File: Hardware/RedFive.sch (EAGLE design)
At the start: 95 parts, among them IC3 LM1117, J1 AVR_SPI_PROG_3X2PTH, J2 USB Female Type C Connector, J3 POWER_JACKSUPER_BOMB_DIGITY, J5 JTAG, Q1 1.1A/60V/600mΩ, U2 1.8V, U3 AP2112-3.3V, U4 FE310, U5 32MB, Y1 32.768KHZ, Y2 16MHz

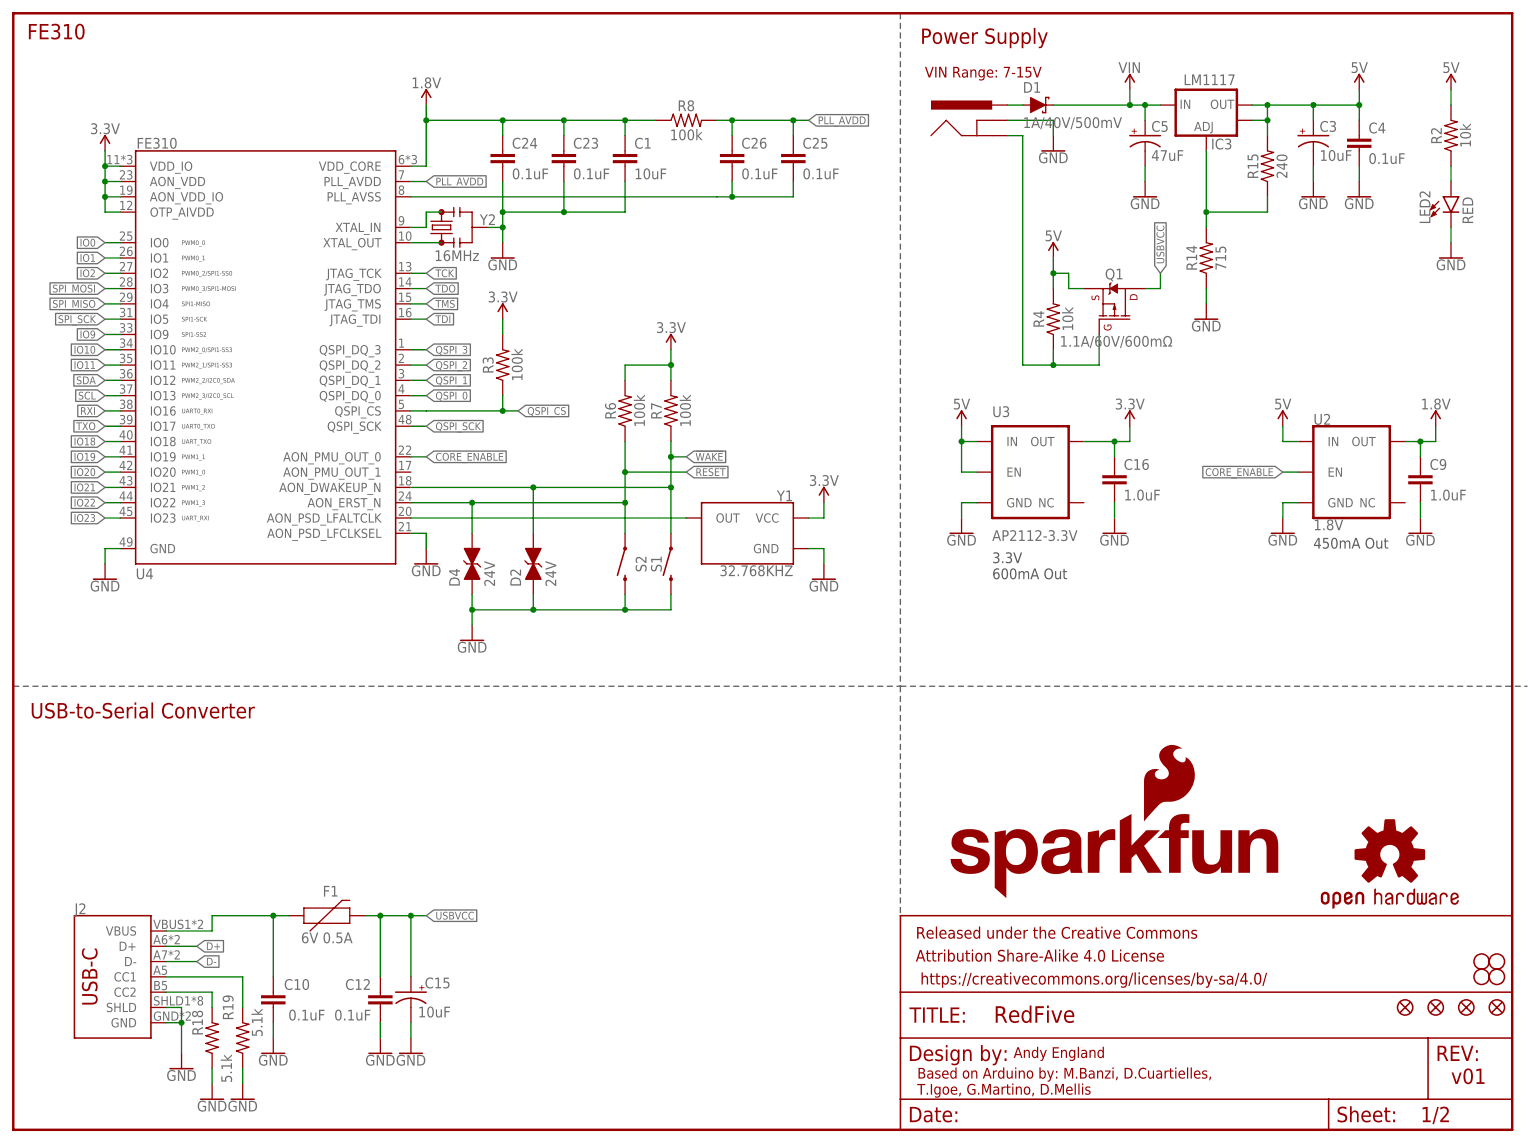
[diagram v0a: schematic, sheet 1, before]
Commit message: small schematic tweaks, thanks pete for notes
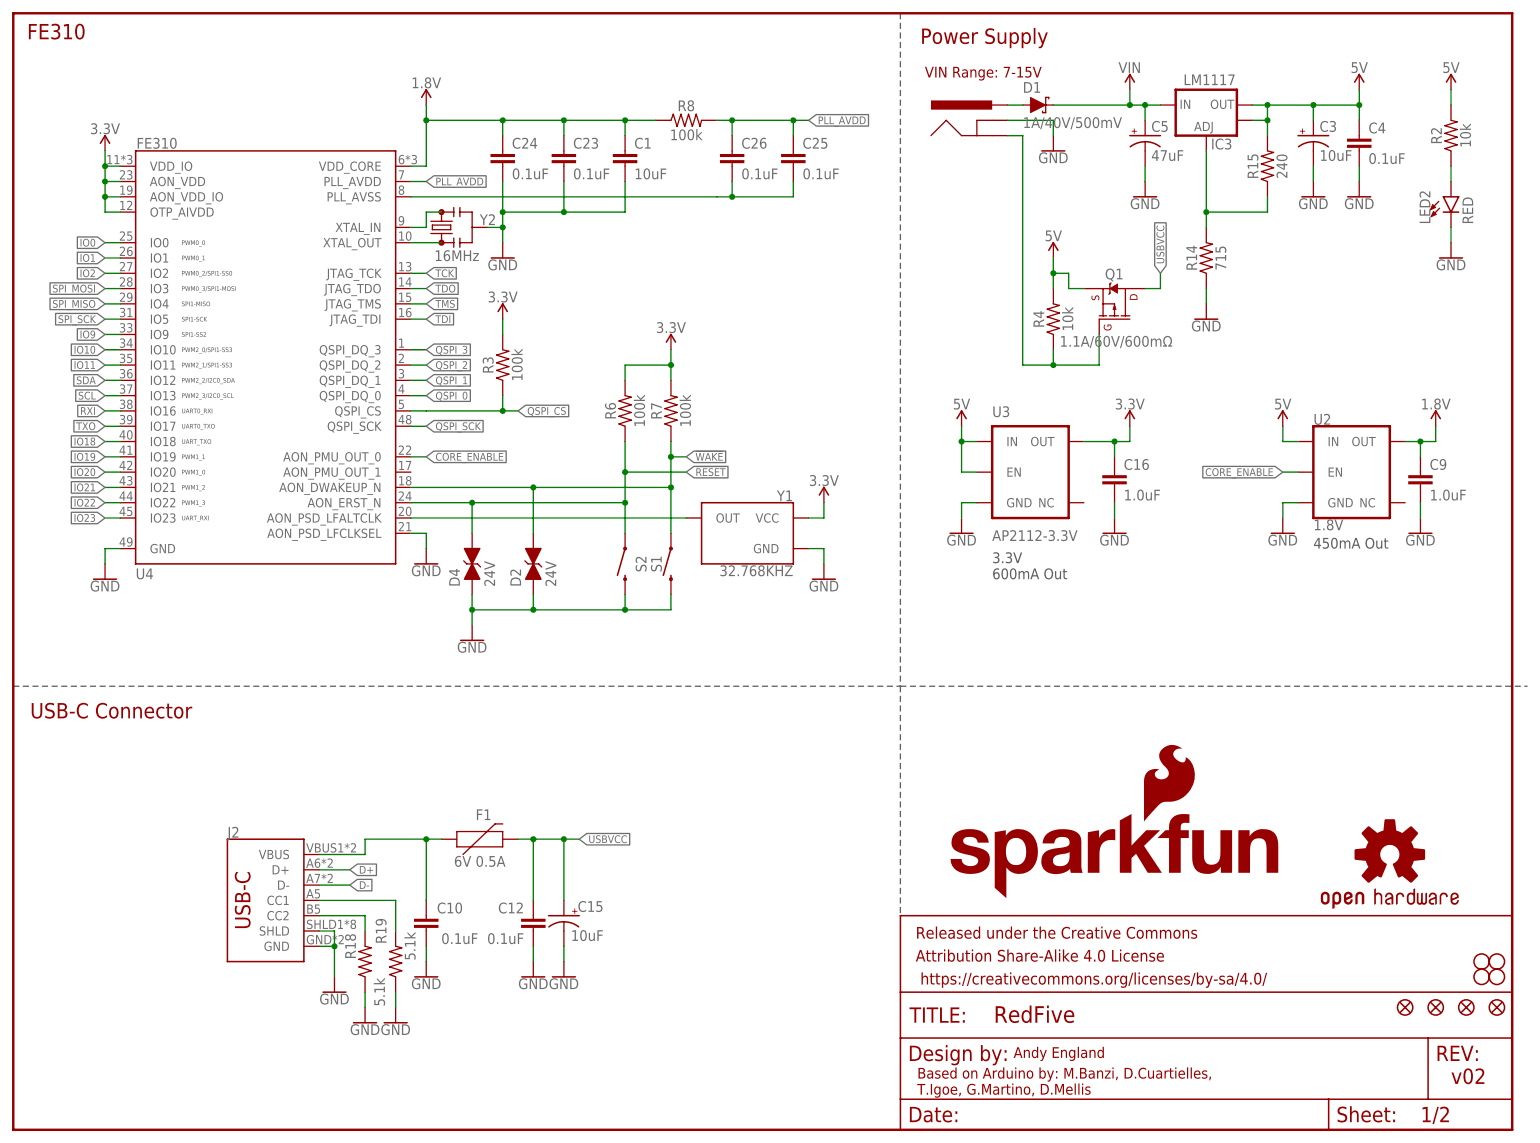
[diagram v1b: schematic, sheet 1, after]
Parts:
- J1: value AVR_SPI_PROG_3X2PTH -> FEMALE 2x3; device SparkFun-Connectors:AVR_SPI_PROG_3X2PTH -> SparkFun-Connectors:CONN_03X2FEMALE
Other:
- note added: "USB-C Connector"
- note removed: "USB-to-Serial Converter"
- note removed: "v01"
- moved on the sheet: C10, C12, C15, F1, J2, R18, R19

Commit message: post design review changes
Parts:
- added JP1: JUMPER-SMT_2_NO_NO-SILK, SparkFun-Jumpers:JUMPER-SMT_2_NO_NO-SILK
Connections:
- net USBVCC: now also JP1.2
- net VUSB: now also JP1.1
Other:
- note added: "Closing this jumper bypasses the .5A fuse. Only close it if you need a lot of current."
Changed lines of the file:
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@@
 <part name="GND27" library="SparkFun-PowerSymbols" deviceset="GND" device=""/>
 <part name="SUPPLY23" library="SparkFun-PowerSymbols" deviceset="3.3V" device=""/>
+<part name="JP1" library="SparkFun-Jumpers" deviceset="JUMPER-SMT_2_NO" device="_NO-SILK"/>
 </parts>
 <sheets>
@@
 <wire x1="147.32" y1="185.42" x2="147.32" y2="73.66" width="0.2032" layer="97" style="longdash"/>
 <text x="215.9" y="96.52" size="1.778" layer="97" font="vector">450mA Out</text>
+<text x="15.24" y="60.96" size="1.778" layer="94" font="vector">Closing this jumper bypasses the .5A fuse. Only close it if you need a lot of current.</text>
 </plain>
 <instances>
@@
 <attribute name="VALUE" x="63.5" y="17.526" size="1.778" layer="96" align="top-center"/>
 </instance>
+<instance part="JP1" gate="G$1" x="76.2" y="55.88"/>
 </instances>
 <busses>
@@
 <pinref part="C15" gate="G$1" pin="+"/>
 <wire x1="83.82" y1="48.26" x2="86.36" y2="48.26" width="0.1524" layer="91"/>
-<wire x1="86.36" y1="48.26" x2="91.44" y2="48.26" width="0.1524" layer="91"/>
+<wire x1="86.36" y1="48.26" x2="88.9" y2="48.26" width="0.1524" layer="91"/>
+<wire x1="88.9" y1="48.26" x2="91.44" y2="48.26" width="0.1524" layer="91"/>
 <wire x1="91.44" y1="38.1" x2="91.44" y2="48.26" width="0.1524" layer="91"/>
 <pinref part="C12" gate="G$1" pin="1"/>
@@
 <wire x1="91.44" y1="48.26" x2="93.98" y2="48.26" width="0.1524" layer="91"/>
 <junction x="91.44" y="48.26"/>
+<pinref part="JP1" gate="G$1" pin="2"/>
+<wire x1="81.28" y1="55.88" x2="88.9" y2="55.88" width="0.1524" layer="91"/>
+<wire x1="88.9" y1="55.88" x2="88.9" y2="48.26" width="0.1524" layer="91"/>
+<junction x="88.9" y="48.26"/>
 </segment>
 </net>
@@
 <wire x1="50.8" y1="45.72" x2="58.42" y2="45.72" width="0.1524" layer="91"/>
 <wire x1="58.42" y1="45.72" x2="58.42" y2="48.26" width="0.1524" layer="91"/>
-<wire x1="58.42" y1="48.26" x2="68.58" y2="48.26" width="0.1524" layer="91"/>
+<wire x1="58.42" y1="48.26" x2="66.04" y2="48.26" width="0.1524" layer="91"/>
 <pinref part="C10" gate="G$1" pin="1"/>
+<wire x1="66.04" y1="48.26" x2="68.58" y2="48.26" width="0.1524" layer="91"/>
 <wire x1="68.58" y1="48.26" x2="71.12" y2="48.26" width="0.1524" layer="91"/>
 <wire x1="68.58" y1="38.1" x2="68.58" y2="48.26" width="0.1524" layer="91"/>
 <junction x="68.58" y="48.26"/>
 <pinref part="J2" gate="J1" pin="VBUS"/>
-</segment>
-</net>
+<wire x1="66.04" y1="48.26" x2="66.04" y2="55.88" width="0.1524" layer="91"/>
+<junction x="66.04" y="48.26"/>
+<pinref part="JP1" gate="G$1" pin="1"/>
+<wire x1="66.04" y1="55.88" x2="71.12" y2="55.88" width="0.1524" layer="91"/>
+</segment>
+</net>

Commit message: post checklist changes, protos ordered
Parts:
- removed TP8: TEST-POINT3, SparkFun-Connectors:TEST-POINT3
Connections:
- net DBG_RESET: no longer TP8.1
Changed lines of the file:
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@@
 <part name="SUPPLY18" library="SparkFun-PowerSymbols" deviceset="3.3V" device=""/>
 <part name="GND24" library="SparkFun-PowerSymbols" deviceset="GND" device=""/>
-<part name="TP8" library="SparkFun-Connectors" deviceset="TEST-POINT" device="3"/>
 <part name="R20" library="SparkFun-Resistors" deviceset="100KOHM" device="-0603-1/10W-1%" value="100k"/>
 <part name="SUPPLY19" library="SparkFun-PowerSymbols" deviceset="3.3V" device=""/>
@@
 <attribute name="VALUE" x="91.44" y="144.526" size="1.778" layer="96" align="top-center"/>
 </instance>
-<instance part="TP8" gate="G$1" x="157.48" y="40.64" smashed="yes" rot="R270">
-<attribute name="NAME" x="157.48" y="43.18" size="1.778" layer="95" font="vector" rot="R270"/>
-</instance>
 <instance part="R20" gate="G$1" x="160.02" y="53.34" smashed="yes" rot="R90">
 <attribute name="NAME" x="158.496" y="53.34" size="1.778" layer="95" font="vector" rot="R90" align="bottom-center"/>
@@
 <wire x1="160.02" y1="45.72" x2="157.48" y2="45.72" width="0.1524" layer="91"/>
 <junction x="160.02" y="45.72"/>
-<pinref part="TP8" gate="G$1" pin="1"/>
-<wire x1="157.48" y1="45.72" x2="157.48" y2="40.64" width="0.1524" layer="91"/>
 <wire x1="157.48" y1="45.72" x2="154.94" y2="45.72" width="0.1524" layer="91"/>
-<junction x="157.48" y="45.72"/>
 <label x="154.94" y="45.72" size="1.27" layer="95" font="vector" rot="R180" xref="yes"/>
 </segment>

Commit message: adding 5V test point
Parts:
- added TP8: TEST-POINT3, SparkFun-Connectors:TEST-POINT3
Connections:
- net 5V: now also TP8.1
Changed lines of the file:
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@@
 <part name="SUPPLY23" library="SparkFun-PowerSymbols" deviceset="3.3V" device=""/>
 <part name="JP1" library="SparkFun-Jumpers" deviceset="JUMPER-SMT_2_NO" device="_NO-SILK"/>
+<part name="TP8" library="SparkFun-Connectors" deviceset="TEST-POINT" device="3"/>
 </parts>
 <sheets>
@@
 <instance part="SUPPLY23" gate="G$1" x="20.32" y="81.28" smashed="yes">
 <attribute name="VALUE" x="20.32" y="84.074" size="1.778" layer="96" align="bottom-center"/>
+</instance>
+<instance part="TP8" gate="G$1" x="66.04" y="20.32" smashed="yes" rot="R180">
+<attribute name="NAME" x="68.58" y="20.32" size="1.778" layer="95" font="vector" rot="R180"/>
 </instance>
 </instances>
@@
 <segment>
 <pinref part="SUPPLY3" gate="G$1" pin="5V"/>
-<wire x1="73.66" y1="27.94" x2="73.66" y2="33.02" width="0.1524" layer="91"/>
 <pinref part="JP10" gate="G$1" pin="4"/>
 <wire x1="73.66" y1="20.32" x2="76.2" y2="20.32" width="0.1524" layer="91"/>
-<wire x1="73.66" y1="20.32" x2="73.66" y2="27.94" width="0.1524" layer="91"/>
-</segment>
-</net>
+<wire x1="73.66" y1="20.32" x2="73.66" y2="33.02" width="0.1524" layer="91"/>
+<pinref part="TP8" gate="G$1" pin="1"/>
+<wire x1="66.04" y1="20.32" x2="73.66" y2="20.32" width="0.1524" layer="91"/>
+<junction x="73.66" y="20.32"/>
+</segment>
+</net>

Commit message: needs routing, post prototype changes
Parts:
- J4: value (none) -> QWIIC_RIGHT_ANGLE
- U5: value 32MB -> 32MBit
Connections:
- net RXI: now also LED3.C, U$44.PTB17; no longer D5.C, U$44.PTB16
- net TXO: now also D5.C, U$44.PTB16; no longer LED3.C, U$44.PTB17
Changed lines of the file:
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@@
 <part name="SUPPLY8" library="SparkFun-PowerSymbols" deviceset="3.3V" device=""/>
 <part name="SUPPLY6" library="SparkFun-PowerSymbols" deviceset="3.3V" device=""/>
-<part name="J4" library="SparkFun-Connectors" deviceset="QWIIC_CONNECTOR" device="JS-1MM"/>
+<part name="J4" library="SparkFun-Connectors" deviceset="QWIIC_CONNECTOR" device="JS-1MM" value="QWIIC_RIGHT_ANGLE"/>
 <part name="GND2" library="SparkFun-PowerSymbols" deviceset="GND" device=""/>
 <part name="FRAME2" library="SparkFun-Aesthetics" deviceset="FRAME-LETTER" device=""/>
@@
 <part name="R3" library="SparkFun-Resistors" deviceset="100KOHM" device="-0603-1/10W-1%" value="100k"/>
 <part name="SUPPLY13" library="SparkFun-PowerSymbols" deviceset="3.3V" device=""/>
-<part name="U5" library="SparkFun-IC-Memory" deviceset="QSPI32MBIT" device="" value="32MB"/>
+<part name="U5" library="SparkFun-IC-Memory" deviceset="QSPI32MBIT" device="" value="32MBit"/>
 <part name="C2" library="SparkFun-Capacitors" deviceset="0.1UF" device="-0603-25V-(+80/-20%)" value="0.1uF"/>
 <part name="GND5" library="SparkFun-PowerSymbols" deviceset="GND" device=""/>
@@
 </segment>
 <segment>
+<label x="238.76" y="114.3" size="1.27" layer="95" font="vector" rot="MR180" xref="yes"/>
+<wire x1="218.44" y1="114.3" x2="236.22" y2="114.3" width="0.1524" layer="91"/>
+<pinref part="LED3" gate="G$1" pin="C"/>
+<wire x1="236.22" y1="114.3" x2="238.76" y2="114.3" width="0.1524" layer="91"/>
+<wire x1="236.22" y1="119.38" x2="236.22" y2="114.3" width="0.1524" layer="91"/>
+<junction x="236.22" y="114.3"/>
+<pinref part="U$44" gate="G$1" pin="PTB17"/>
+</segment>
+</net>
+<net name="TXO" class="0">
+<segment>
+<wire x1="43.18" y1="27.94" x2="40.64" y2="27.94" width="0.1524" layer="91"/>
+<pinref part="JP11" gate="G$1" pin="2"/>
+<label x="40.64" y="27.94" size="1.27" layer="95" font="vector" rot="R180" xref="yes"/>
+</segment>
+<segment>
 <wire x1="218.44" y1="116.84" x2="226.06" y2="116.84" width="0.1524" layer="91"/>
 <label x="238.76" y="116.84" size="1.27" layer="95" font="vector" xref="yes"/>
@@
 </segment>
 </net>
-<net name="TXO" class="0">
-<segment>
-<wire x1="43.18" y1="27.94" x2="40.64" y2="27.94" width="0.1524" layer="91"/>
-<pinref part="JP11" gate="G$1" pin="2"/>
-<label x="40.64" y="27.94" size="1.27" layer="95" font="vector" rot="R180" xref="yes"/>
-</segment>
-<segment>
-<label x="238.76" y="114.3" size="1.27" layer="95" font="vector" rot="MR180" xref="yes"/>
-<wire x1="218.44" y1="114.3" x2="236.22" y2="114.3" width="0.1524" layer="91"/>
-<pinref part="LED3" gate="G$1" pin="C"/>
-<wire x1="236.22" y1="114.3" x2="238.76" y2="114.3" width="0.1524" layer="91"/>
-<wire x1="236.22" y1="119.38" x2="236.22" y2="114.3" width="0.1524" layer="91"/>
-<junction x="236.22" y="114.3"/>
-<pinref part="U$44" gate="G$1" pin="PTB17"/>
-</segment>
-</net>
